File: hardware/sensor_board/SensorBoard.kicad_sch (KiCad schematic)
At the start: 22 parts, among them J1 EXT PORT, J10 LED L1, J11 LED R3, J12 LED R2, J13 LED R1, J14 HX711 L, J15 HX711 R, J2 TARE L, J3 TARE R, J4 SOIL SENSOR L, J5 SOIL SENSOR R, J6 DHT22 L, J7 DHT22 R, J8 LED L3, J9 LED L2, U1 Pico

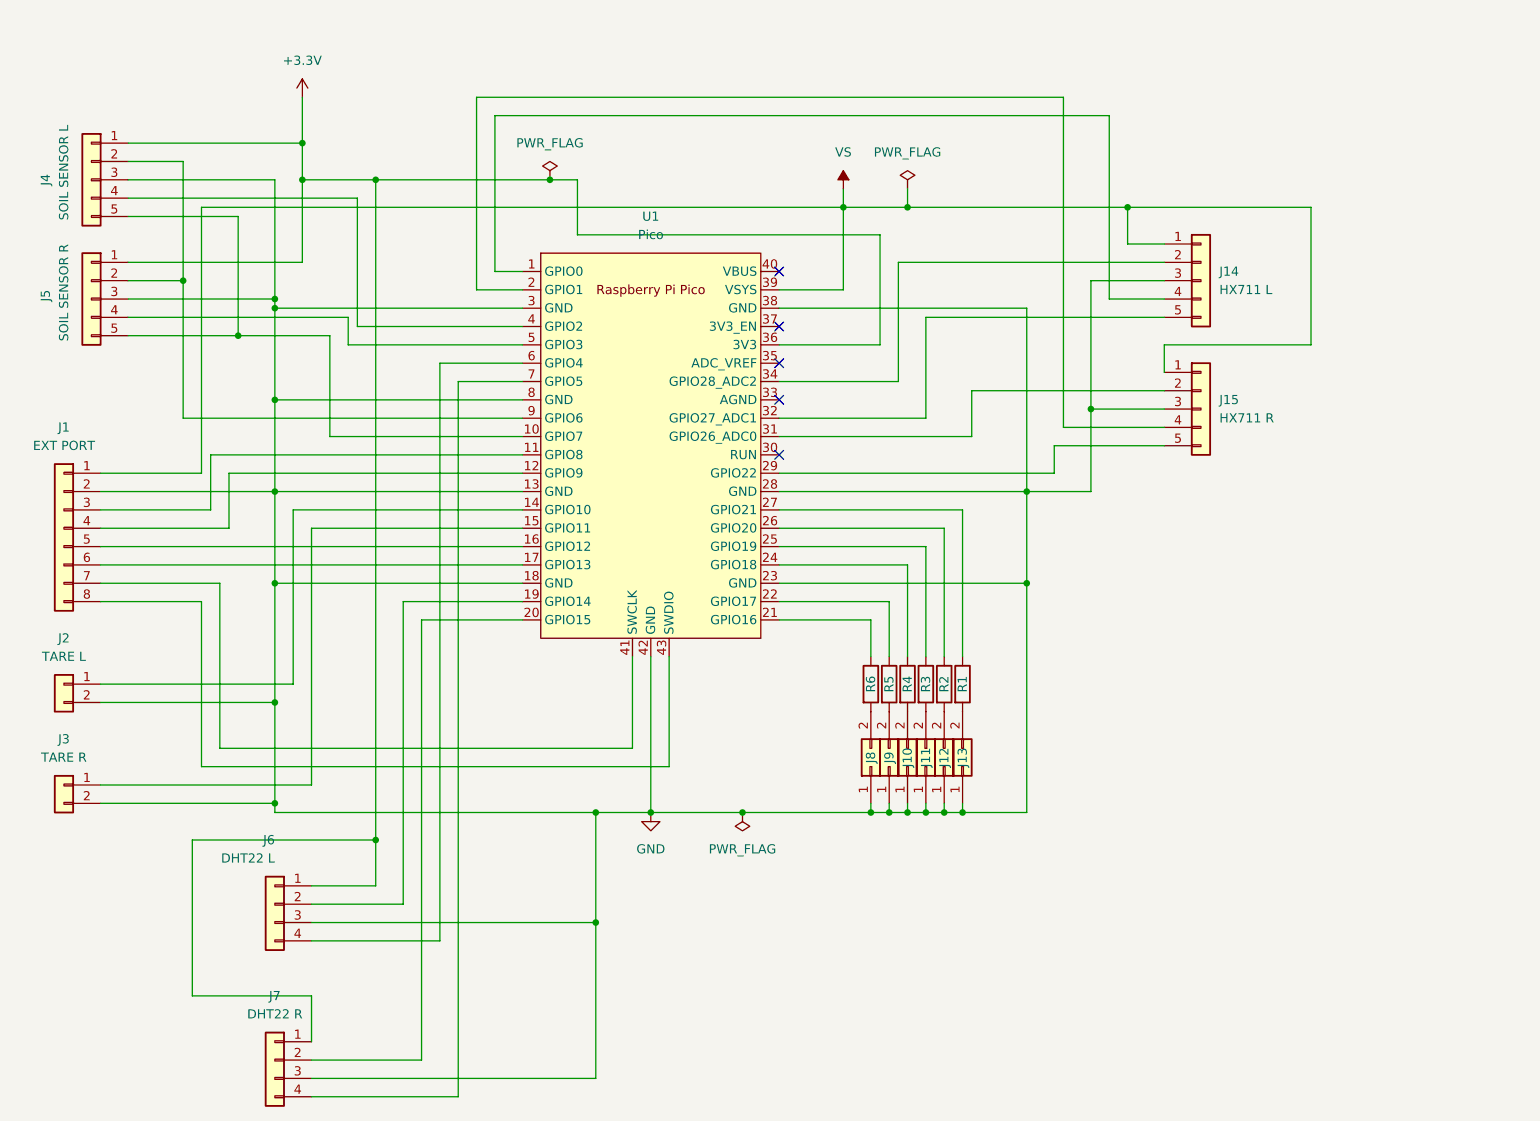
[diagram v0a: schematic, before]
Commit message: PCB v2.0. Using sonars instead of load cells, which frees up the tare buttons. Also using a shift register for LEDs instead of direct GPIO control which frees up three more pins.
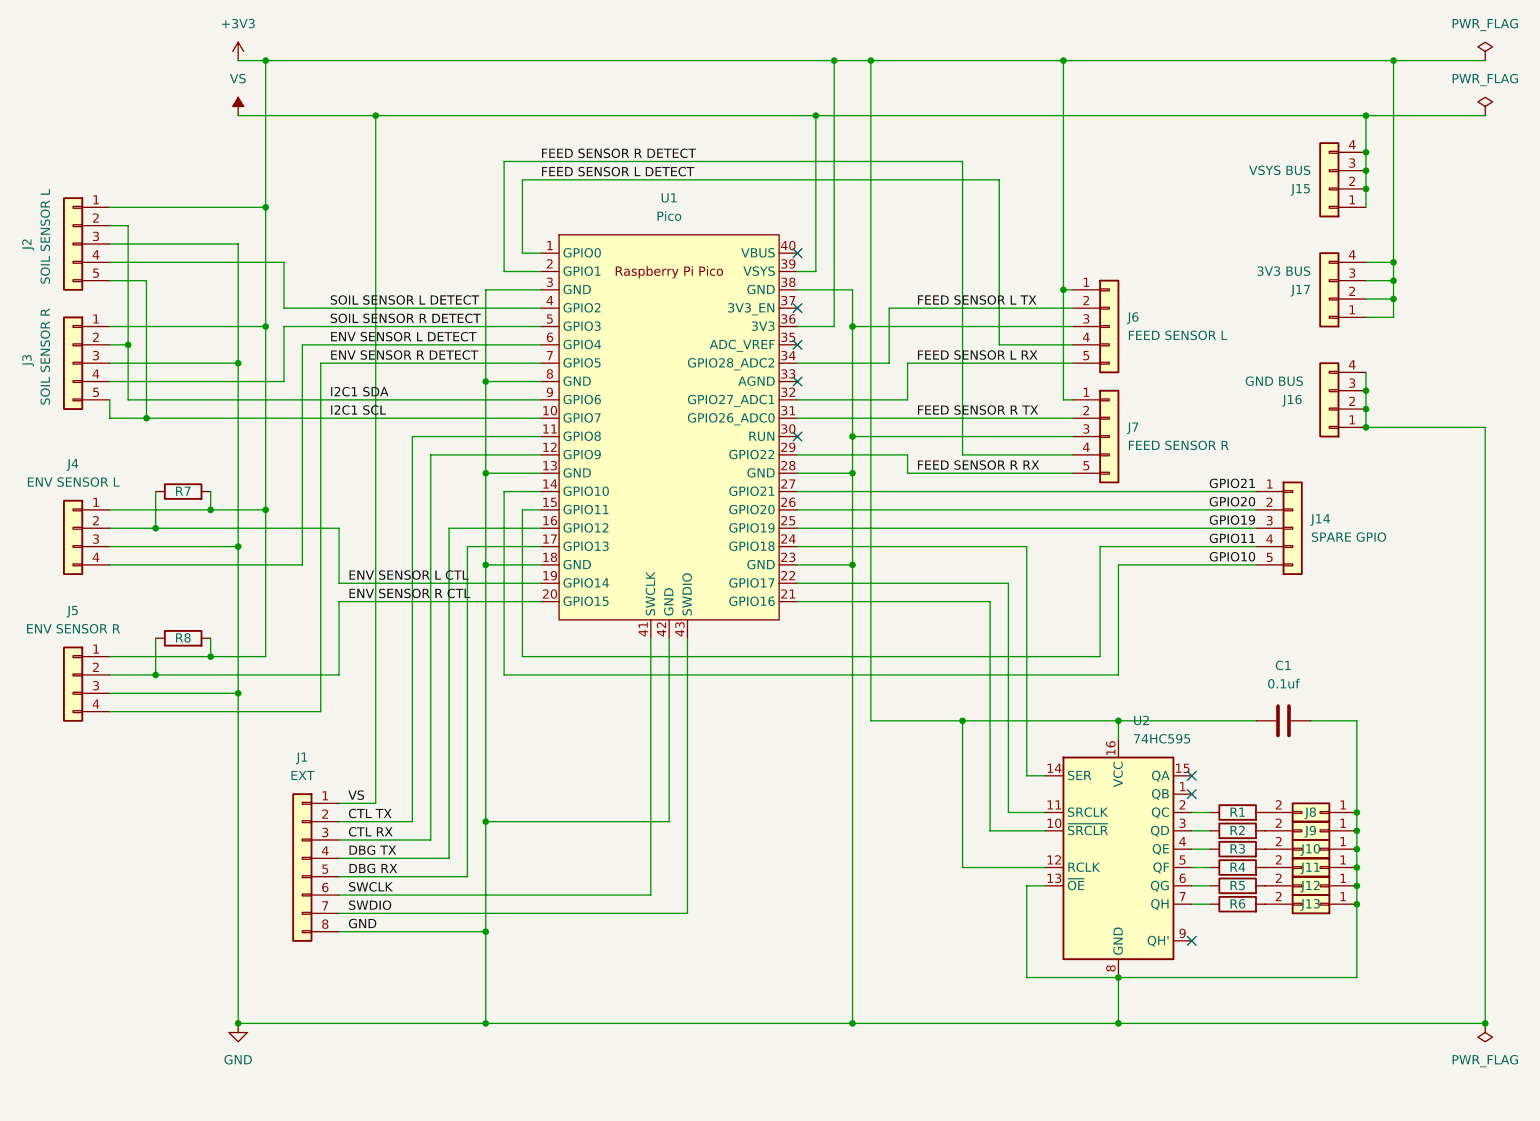
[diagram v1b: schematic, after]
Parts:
- removed J2: TARE L, Connector_JST:JST_EH_B2B-EH-A_1x02_P2.50mm_Vertical, symbol Connector_Generic:Conn_01x02
- removed J3: TARE R, Connector_JST:JST_EH_B2B-EH-A_1x02_P2.50mm_Vertical, symbol Connector_Generic:Conn_01x02
- added C1: 0.1uf, Capacitor_THT:C_Disc_D6.0mm_W2.5mm_P5.00mm, symbol Device:C
- added J14: SPARE GPIO, Connector_PinHeader_2.54mm:PinHeader_1x05_P2.54mm_Vertical, symbol Connector_Generic:Conn_01x05
- added J15: VSYS BUS, Connector_PinHeader_2.54mm:PinHeader_1x04_P2.54mm_Vertical, symbol Connector_Generic:Conn_01x04
- added J16: GND BUS, Connector_PinHeader_2.54mm:PinHeader_1x04_P2.54mm_Vertical, symbol Connector_Generic:Conn_01x04
- added J17: 3V3 BUS, Connector_PinHeader_2.54mm:PinHeader_1x04_P2.54mm_Vertical, symbol Connector_Generic:Conn_01x04
- added R7: R7, Resistor_THT:R_Axial_DIN0207_L6.3mm_D2.5mm_P7.62mm_Horizontal, symbol Device:R
- added R8: R8, Resistor_THT:R_Axial_DIN0207_L6.3mm_D2.5mm_P7.62mm_Horizontal, symbol Device:R
- added U2: 74HC595, Package_DIP:DIP-16_W7.62mm, symbol 74xx:74HC595
- J1: value EXT PORT -> EXT; footprint Connector_JST:JST_EH_B8B-EH-A_1x08_P2.50mm_Vertical -> Connector_JST:JST_XH_B8B-XH-A_1x08_P2.50mm_Vertical
- J10: renamed from J11; value LED R3 -> LED L2; footprint Connector_JST:JST_EH_B2B-EH-A_1x02_P2.50mm_Vertical -> Connector_JST:JST_XH_B2B-XH-A_1x02_P2.50mm_Vertical
- J11: renamed from J10; value LED L1 -> LED L3; footprint Connector_JST:JST_EH_B2B-EH-A_1x02_P2.50mm_Vertical -> Connector_JST:JST_XH_B2B-XH-A_1x02_P2.50mm_Vertical
- J12: renamed from J9; value LED L2 -> LED R1; footprint Connector_JST:JST_EH_B2B-EH-A_1x02_P2.50mm_Vertical -> Connector_JST:JST_XH_B2B-XH-A_1x02_P2.50mm_Vertical
- J13: renamed from J8; value LED L3 -> LED R2; footprint Connector_JST:JST_EH_B2B-EH-A_1x02_P2.50mm_Vertical -> Connector_JST:JST_XH_B2B-XH-A_1x02_P2.50mm_Vertical
- J2: renamed from J4; footprint Connector_JST:JST_EH_B5B-EH-A_1x05_P2.50mm_Vertical -> Connector_JST:JST_XH_B5B-XH-A_1x05_P2.50mm_Vertical
- J3: renamed from J5; footprint Connector_JST:JST_EH_B5B-EH-A_1x05_P2.50mm_Vertical -> Connector_JST:JST_XH_B5B-XH-A_1x05_P2.50mm_Vertical
- J4: renamed from J6; value DHT22 L -> ENV SENSOR L; footprint Connector_JST:JST_EH_B4B-EH-A_1x04_P2.50mm_Vertical -> Connector_JST:JST_XH_B4B-XH-A_1x04_P2.50mm_Vertical
- J5: renamed from J7; value DHT22 R -> ENV SENSOR R; footprint Connector_JST:JST_EH_B4B-EH-A_1x04_P2.50mm_Vertical -> Connector_JST:JST_XH_B4B-XH-A_1x04_P2.50mm_Vertical
- J6: renamed from J14; value HX711 L -> FEED SENSOR L; footprint Connector_JST:JST_EH_B5B-EH-A_1x05_P2.50mm_Vertical -> Connector_JST:JST_XH_B5B-XH-A_1x05_P2.50mm_Vertical
- J7: renamed from J15; value HX711 R -> FEED SENSOR R; footprint Connector_JST:JST_EH_B5B-EH-A_1x05_P2.50mm_Vertical -> Connector_JST:JST_XH_B5B-XH-A_1x05_P2.50mm_Vertical
- J8: renamed from J13; value LED R1 -> LED R3; footprint Connector_JST:JST_EH_B2B-EH-A_1x02_P2.50mm_Vertical -> Connector_JST:JST_XH_B2B-XH-A_1x02_P2.50mm_Vertical
- J9: renamed from J12; value LED R2 -> LED L1; footprint Connector_JST:JST_EH_B2B-EH-A_1x02_P2.50mm_Vertical -> Connector_JST:JST_XH_B2B-XH-A_1x02_P2.50mm_Vertical
- R1: value 150 -> R1
- R2: value 150 -> R2
- R3: value 150 -> R3
- R4: value 150 -> R4
- R5: value 150 -> R5
- R6: value 150 -> R6
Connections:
- net GND: now also J1.8 (Pin_8), C1.2, J16.1 (Pin_1), J16.2 (Pin_2), J16.3 (Pin_3), J16.4 (Pin_4), U2.13 (~{OE}), U2.8 (GND); no longer J1.2 (Pin_2)
- net VS: now also J15.1 (Pin_1), J15.2 (Pin_2), J15.3 (Pin_3), J15.4 (Pin_4); no longer J6.1 (Pin_1), J7.1 (Pin_1)
- net GPIO11: now reaches U1.15 (GPIO11)
- net GPIO11: now also J14.4 (Pin_4)
- net CTL RX: now reaches J1.3 (Pin_3)
- net CTL RX: now also U1.12 (GPIO9); no longer U1.11 (GPIO8)
- net DBG TX: now reaches J1.4 (Pin_4)
- net DBG TX: now also U1.16 (GPIO12); no longer U1.12 (GPIO9)
- net DBG RX: now reaches J1.5 (Pin_5)
- net DBG RX: now also U1.17 (GPIO13); no longer U1.16 (GPIO12)
- net SWCLK: now reaches J1.6 (Pin_6)
- net SWCLK: now also U1.41 (SWCLK); no longer U1.17 (GPIO13)
- net SWDIO: now reaches J1.7 (Pin_7)
- net SWDIO: now also U1.43 (SWDIO); no longer U1.41 (SWCLK)
- net at U1.21 (GPIO16): now also U2.10 (~{SRCLR}); no longer R6.1
- net FEED SENSOR R TX: now reaches J7.2 (Pin_2), U1.31 (GPIO26_ADC0)
- net FEED SENSOR R DETECT: now reaches J7.4 (Pin_4), U1.2 (GPIO1)
- net FEED SENSOR R RX: now reaches J7.5 (Pin_5), U1.29 (GPIO22)
- net ENV SENSOR R CTL: now reaches J5.2 (Pin_2), U1.20 (GPIO15)
- net ENV SENSOR R CTL: now also R8.1
- net ENV SENSOR R DETECT: now reaches J5.4 (Pin_4), U1.7 (GPIO5)
- net FEED SENSOR L TX: now reaches J6.2 (Pin_2), U1.34 (GPIO28_ADC2)
- net FEED SENSOR L DETECT: now reaches J6.4 (Pin_4), U1.1 (GPIO0)
- net FEED SENSOR L RX: now reaches J6.5 (Pin_5), U1.32 (GPIO27_ADC1)
- net I2C1 SDA: now reaches J2.2 (Pin_2), J3.2 (Pin_2), U1.9 (GPIO6)
- net SOIL SENSOR R DETECT: now reaches J3.4 (Pin_4), U1.5 (GPIO3)
- net I2C1 SCL: now reaches J2.5 (Pin_5), J3.5 (Pin_5), U1.10 (GPIO7)
- net at U1.22 (GPIO17): now also U2.11 (SRCLK); no longer R5.1
- net GPIO10: now reaches U1.14 (GPIO10)
- net GPIO10: now also J14.5 (Pin_5)
- net ENV SENSOR L CTL: now reaches J4.2 (Pin_2), U1.19 (GPIO14)
- net ENV SENSOR L CTL: now also R7.1
- net ENV SENSOR L DETECT: now reaches J4.4 (Pin_4), U1.6 (GPIO4)
- net at R2.1: now also U2.3 (QD); no longer U1.26 (GPIO20)
- net at R3.1: now also U2.4 (QE); no longer U1.25 (GPIO19)
- net at R1.1: now also U2.2 (QC); no longer U1.27 (GPIO21)
- net SOIL SENSOR L DETECT: now reaches J2.4 (Pin_4), U1.4 (GPIO2)
- net at U1.24 (GPIO18): now also U2.14 (SER); no longer R4.1
- net +3.3V renamed +3V3
- net +3V3: now also J6.1 (Pin_1), J7.1 (Pin_1), C1.1, J17.1 (Pin_1), J17.2 (Pin_2), J17.3 (Pin_3), J17.4 (Pin_4), R7.2, R8.2, U2.12 (RCLK), U2.16 (VCC)
- new net: R4.1, U2.5 (QF)
- new net: R5.1, U2.6 (QG)
- new net: R6.1, U2.7 (QH)
- new net CTL TX: J1.2 (Pin_2), U1.11 (GPIO8)
- new net GPIO19: J14.3 (Pin_3), U1.25 (GPIO19)
- new net GPIO20: J14.2 (Pin_2), U1.26 (GPIO20)
- new net GPIO21: J14.1 (Pin_1), U1.27 (GPIO21)
- no-connect marks 5 -> 8
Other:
- moved on the sheet: J1, J10, J11, J12, J13, J2, J3, J4, J5, J6, J7, J8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

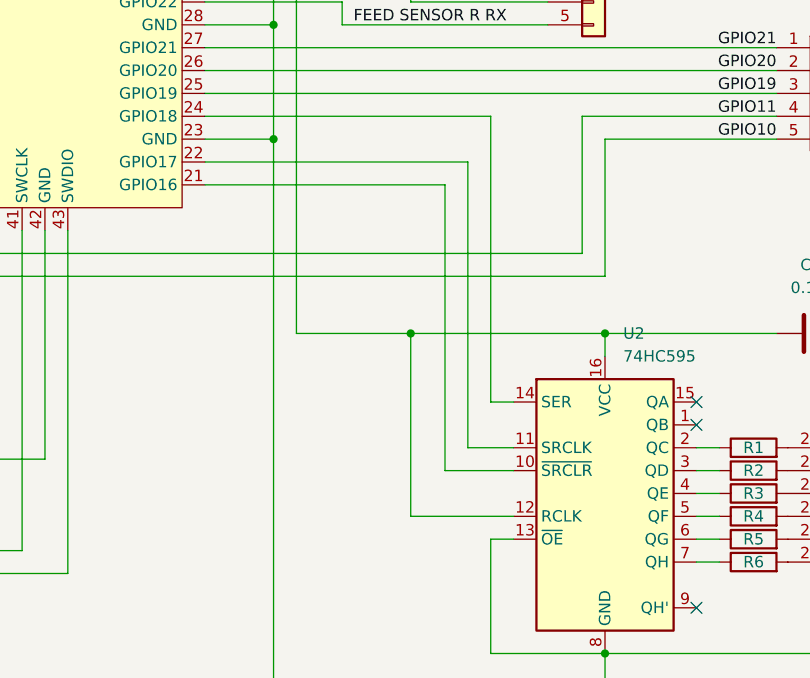
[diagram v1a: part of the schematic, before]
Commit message: Fixed error in shift register wiring
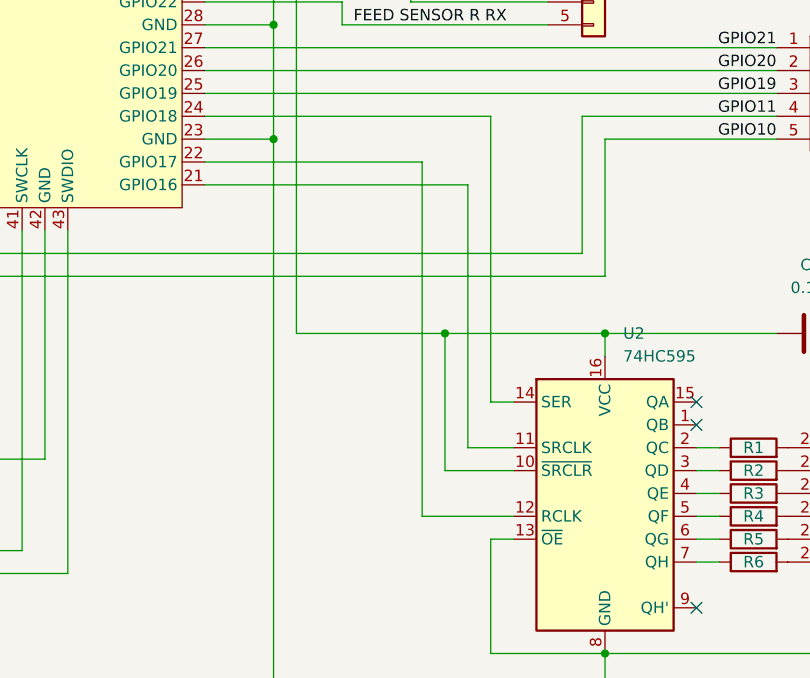
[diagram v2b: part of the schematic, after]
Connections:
- net +3V3: now also U2.10 (~{SRCLR}); no longer U2.12 (RCLK)
- net at U1.21 (GPIO16): now also U2.11 (SRCLK); no longer U2.10 (~{SRCLR})
- net at U1.22 (GPIO17): now also U2.12 (RCLK); no longer U2.11 (SRCLK)
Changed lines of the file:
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@@
   (junction (at 71.12 29.21) (diameter 0) (color 0 0 0 0)
   )
-  (junction (at 152.4 113.03) (diameter 0) (color 0 0 0 0)
-  )
   (junction (at 55.88 21.59) (diameter 0) (color 0 0 0 0)
   )
@@
   )
   (junction (at 207.01 130.81) (diameter 0) (color 0 0 0 0)
+  )
+  (junction (at 156.21 113.03) (diameter 0) (color 0 0 0 0)
   )
   (junction (at 207.01 133.35) (diameter 0) (color 0 0 0 0)
@@
     (stroke (width 0) (type default) (color 0 0 0 0))
   )
-  (wire (pts (xy 163.83 133.35) (xy 152.4 133.35))
-    (stroke (width 0) (type default) (color 0 0 0 0))
-  )
   (wire (pts (xy 137.16 58.42) (xy 137.16 73.66))
     (stroke (width 0) (type default) (color 0 0 0 0))
@@
     (stroke (width 0) (type default) (color 0 0 0 0))
   )
+  (wire (pts (xy 129.54 96.52) (xy 158.75 96.52))
+    (stroke (width 0) (type default) (color 0 0 0 0))
+  )
+  (wire (pts (xy 158.75 96.52) (xy 158.75 125.73))
+    (stroke (width 0) (type default) (color 0 0 0 0))
+  )
   (wire (pts (xy 40.64 101.6) (xy 40.64 106.68))
     (stroke (width 0) (type default) (color 0 0 0 0))
@@
     (stroke (width 0) (type default) (color 0 0 0 0))
   )
+  (wire (pts (xy 153.67 93.98) (xy 153.67 133.35))
+    (stroke (width 0) (type default) (color 0 0 0 0))
+  )
   (wire (pts (xy 39.37 52.07) (xy 39.37 71.12))
     (stroke (width 0) (type default) (color 0 0 0 0))
@@
     (stroke (width 0) (type default) (color 0 0 0 0))
   )
-  (wire (pts (xy 129.54 93.98) (xy 158.75 93.98))
+  (wire (pts (xy 156.21 128.27) (xy 156.21 113.03))
     (stroke (width 0) (type default) (color 0 0 0 0))
   )
@@
     (stroke (width 0) (type default) (color 0 0 0 0))
   )
+  (wire (pts (xy 153.67 133.35) (xy 163.83 133.35))
+    (stroke (width 0) (type default) (color 0 0 0 0))
+  )
   (wire (pts (xy 129.54 78.74) (xy 137.16 78.74))
     (stroke (width 0) (type default) (color 0 0 0 0))
@@
     (stroke (width 0) (type default) (color 0 0 0 0))
   )
-  (wire (pts (xy 158.75 93.98) (xy 158.75 125.73))
-    (stroke (width 0) (type default) (color 0 0 0 0))
-  )
   (wire (pts (xy 34.29 91.44) (xy 60.96 91.44))
     (stroke (width 0) (type default) (color 0 0 0 0))
@@
     (stroke (width 0) (type default) (color 0 0 0 0))
   )
-  (wire (pts (xy 152.4 113.03) (xy 152.4 133.35))
-    (stroke (width 0) (type default) (color 0 0 0 0))
-  )
   (wire (pts (xy 129.54 76.2) (xy 144.78 76.2))
     (stroke (width 0) (type default) (color 0 0 0 0))
@@
     (stroke (width 0) (type default) (color 0 0 0 0))
   )
-  (wire (pts (xy 129.54 96.52) (xy 156.21 96.52))
-    (stroke (width 0) (type default) (color 0 0 0 0))
-  )
   (wire (pts (xy 173.99 91.44) (xy 173.99 106.68))
     (stroke (width 0) (type default) (color 0 0 0 0))
@@
     (stroke (width 0) (type default) (color 0 0 0 0))
   )
-  (wire (pts (xy 139.7 113.03) (xy 152.4 113.03))
+  (wire (pts (xy 139.7 113.03) (xy 156.21 113.03))
     (stroke (width 0) (type default) (color 0 0 0 0))
   )
@@
     (stroke (width 0) (type default) (color 0 0 0 0))
   )
+  (wire (pts (xy 156.21 113.03) (xy 173.99 113.03))
+    (stroke (width 0) (type default) (color 0 0 0 0))
+  )
   (wire (pts (xy 129.54 68.58) (xy 144.78 68.58))
     (stroke (width 0) (type default) (color 0 0 0 0))
@@
     (stroke (width 0) (type default) (color 0 0 0 0))
   )
-  (wire (pts (xy 156.21 96.52) (xy 156.21 128.27))
-    (stroke (width 0) (type default) (color 0 0 0 0))
-  )
   (wire (pts (xy 184.15 138.43) (xy 186.69 138.43))
     (stroke (width 0) (type default) (color 0 0 0 0))
@@
     (stroke (width 0) (type default) (color 0 0 0 0))
   )
-  (wire (pts (xy 152.4 113.03) (xy 173.99 113.03))
-    (stroke (width 0) (type default) (color 0 0 0 0))
-  )
   (wire (pts (xy 78.74 76.2) (xy 78.74 129.54))
     (stroke (width 0) (type default) (color 0 0 0 0))
@@
     (stroke (width 0) (type default) (color 0 0 0 0))
   )
+  (wire (pts (xy 163.83 128.27) (xy 156.21 128.27))
+    (stroke (width 0) (type default) (color 0 0 0 0))
+  )
   (wire (pts (xy 207.01 138.43) (xy 207.01 148.59))
     (stroke (width 0) (type default) (color 0 0 0 0))
@@
     (stroke (width 0) (type default) (color 0 0 0 0))
   )
+  (wire (pts (xy 129.54 93.98) (xy 153.67 93.98))
+    (stroke (width 0) (type default) (color 0 0 0 0))
+  )
   (wire (pts (xy 86.36 127) (xy 111.76 127))
     (stroke (width 0) (type default) (color 0 0 0 0))
@@
     (stroke (width 0) (type default) (color 0 0 0 0))
   )
-  (wire (pts (xy 156.21 128.27) (xy 163.83 128.27))
-    (stroke (width 0) (type default) (color 0 0 0 0))
-  )
